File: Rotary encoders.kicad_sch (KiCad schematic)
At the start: 0 parts

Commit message: added encoder input connector
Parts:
- added C76, C77, C78: 100nF, 0_capacitors:C_0402_1005Metric, symbol 0_capacitors:CL05B104KO5NNNC
- added R69, R70, R71, R72: 10kΩ, 0_resistors:R_0402_1005Metric, symbol 0_resistors:0402WGF1002TCE
- added R73: 5.1kΩ, 0_resistors:R_0402_1005Metric, symbol 0_resistors:0402WGF5101TCE
- added R74: 47kΩ, 0_resistors:R_0402_1005Metric, symbol 0_resistors:0402WGF4702TCE
- added SW9: RotaryEncoder_Switch, Connector_JST:JST_PH_B5B-PH-K_1x05_P2.00mm_Vertical, symbol 0_modules:RotaryEncoder_Switch
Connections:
- new net: R70.2, R72.2, SW9.B
- new net: C78.1, R73.2, R74.2, SW9.S1
- new net: R69.2, R71.2, SW9.A
- new net +3.3V: R69.1, R70.1, R74.1
- new net BUTTON_ENCODER: R73.1
- new net GND: C76.2, C77.2, C78.2, SW9.C, SW9.S2
- new net TIM2_CH1: C76.1, R72.1
- new net TIM2_CH2: C77.1, R71.1
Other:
- title: (none) -> UI - Rotary encoders

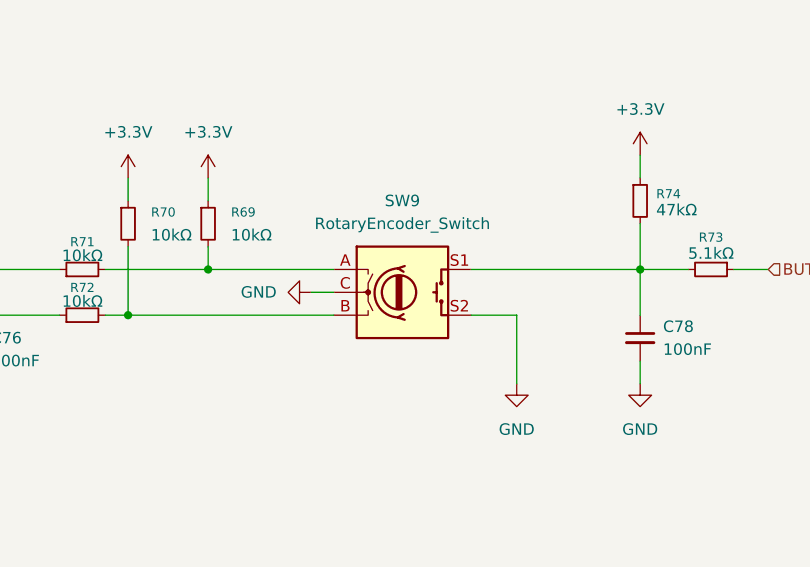
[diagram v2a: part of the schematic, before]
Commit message: duzo zmian, layout przetwornic i zasilania, wstepny routing sd card impedance control, usb differential impedance control
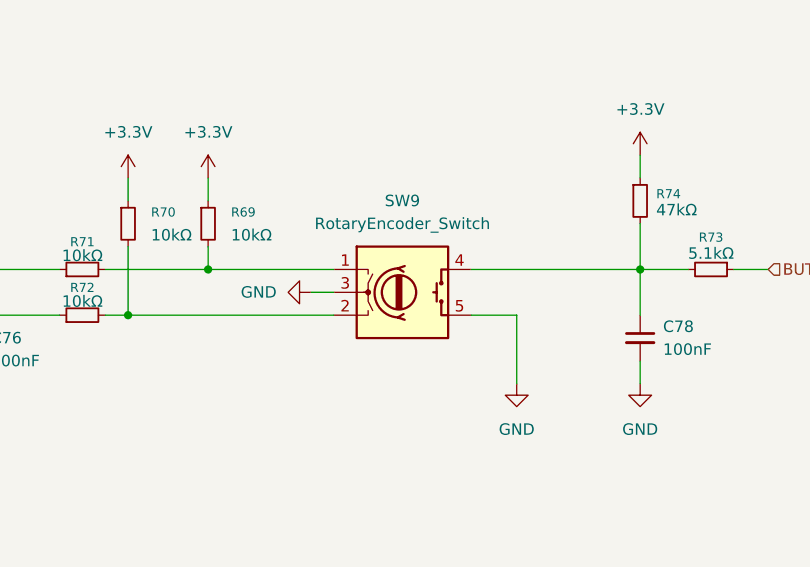
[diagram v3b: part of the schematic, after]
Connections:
- net GND: now also SW9.3, SW9.5; no longer SW9.C, SW9.S2
- net at R70.2, R72.2: now also SW9.2; no longer SW9.B
- net at C78.1, R73.2, R74.2: now also SW9.4; no longer SW9.S1
- net at R69.2, R71.2: now also SW9.1; no longer SW9.A
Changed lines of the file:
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@@
 			)
 		)
-		(pin "A"
+		(pin "3"
 		)
-		(pin "B"
+		(pin "2"
 		)
-		(pin "S2"
+		(pin "4"
 		)
-		(pin "C"
+		(pin "1"
 		)
-		(pin "S1"
+		(pin "5"
 		)
 		(instances

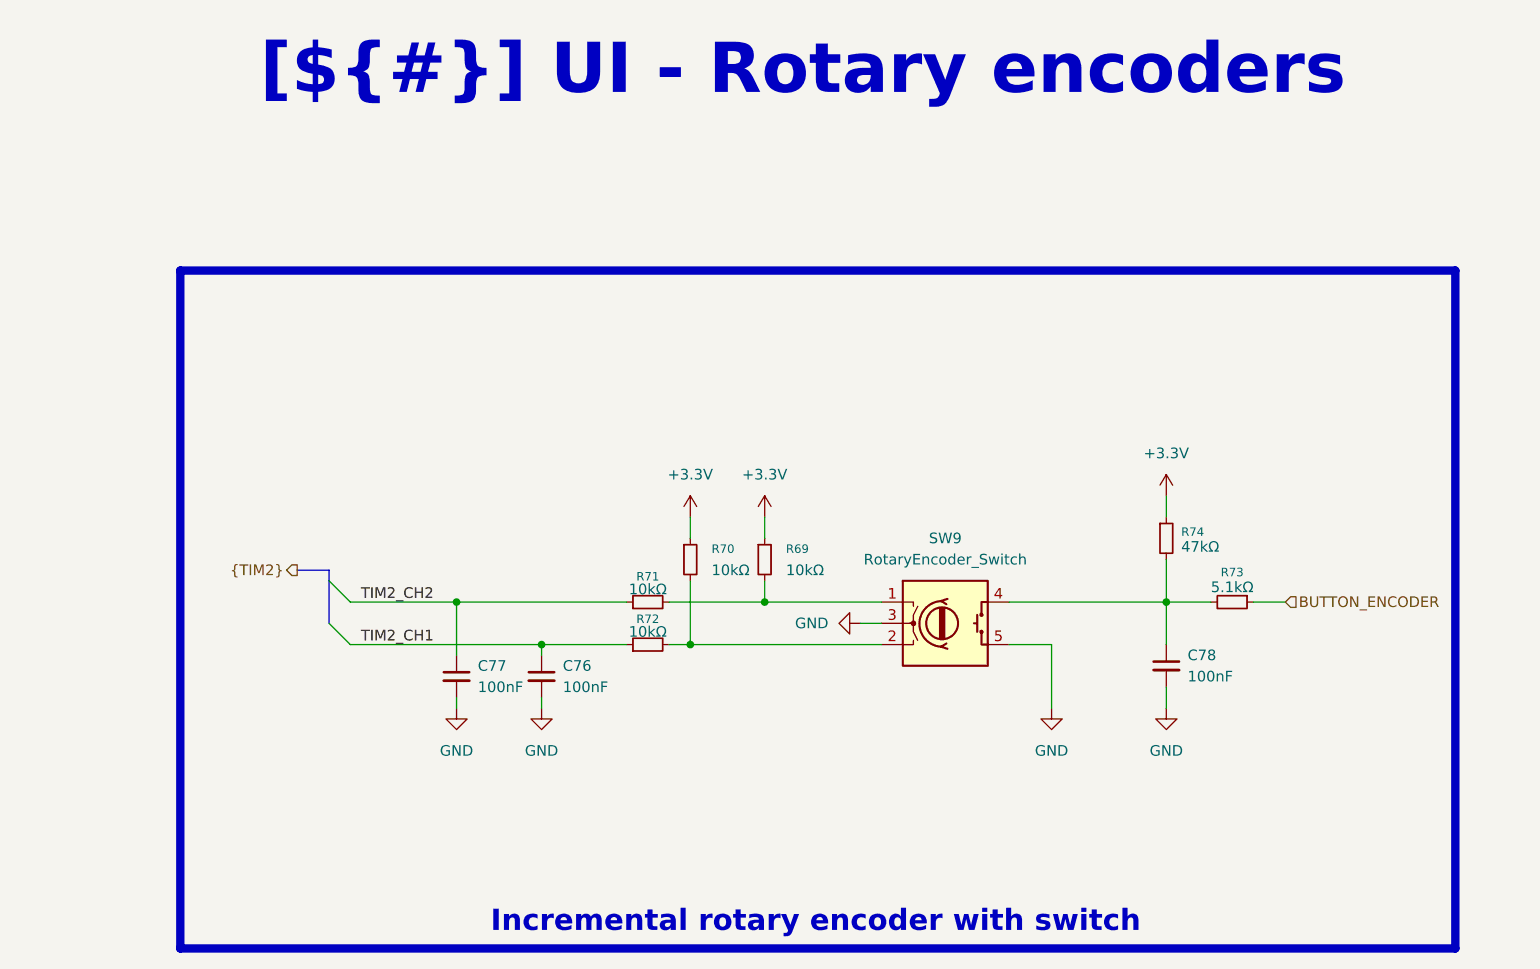
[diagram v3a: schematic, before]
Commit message: added tvs diodes to protect inputs + final component placement
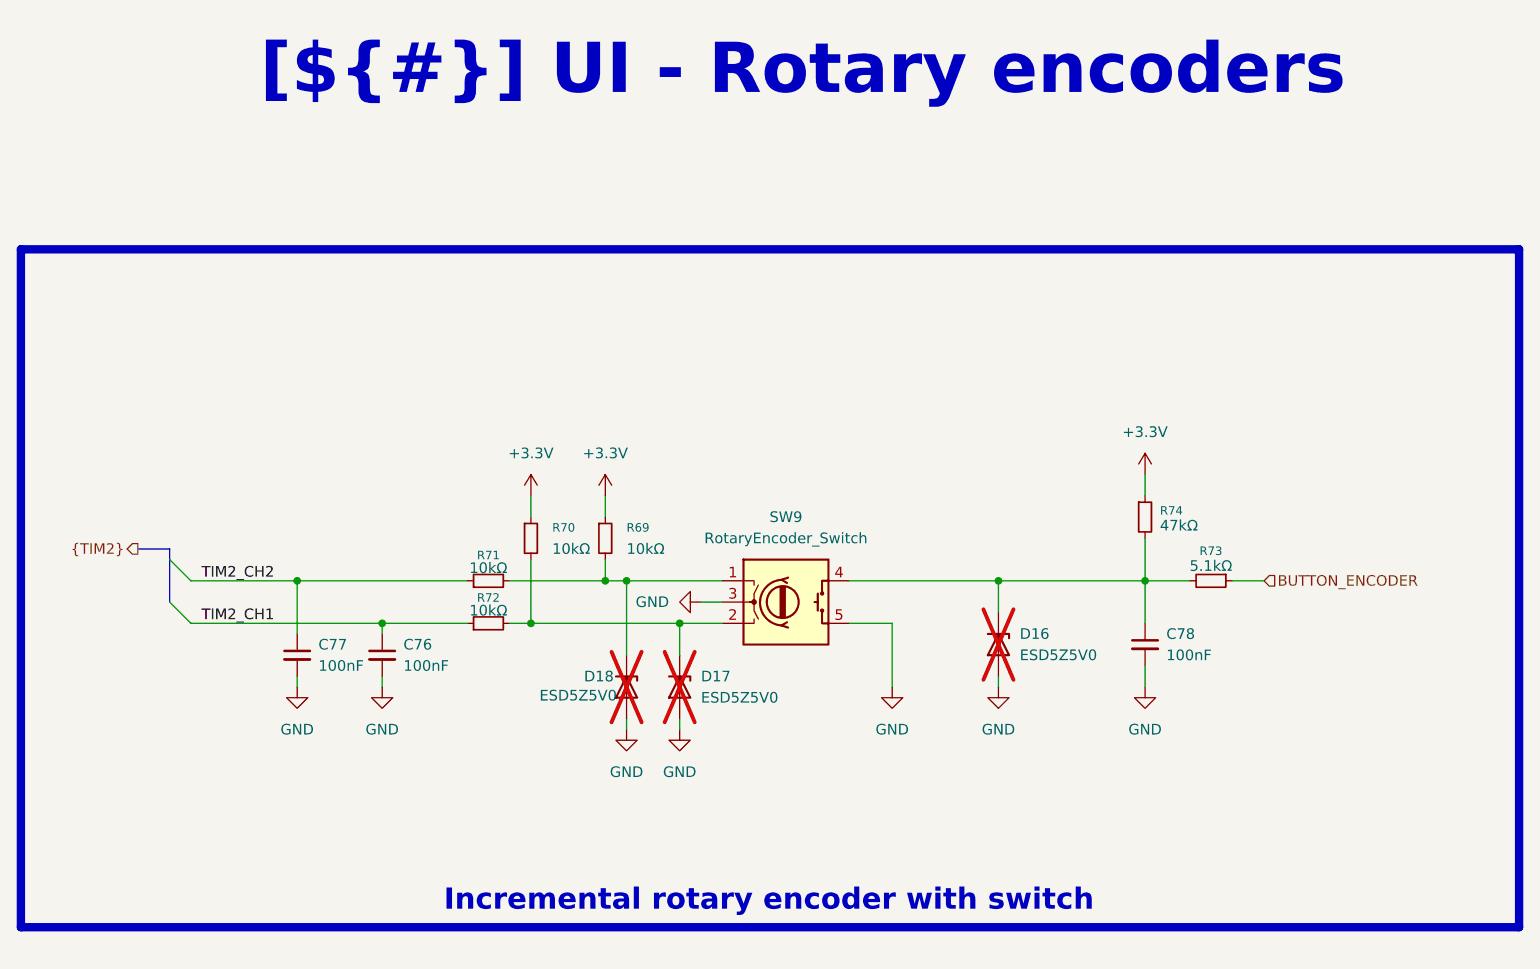
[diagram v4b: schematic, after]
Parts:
- added D16, D17, D18: ESD5Z5V0, 0_diodes:D_SOD-523, symbol 0_diodes:ESD5Z5V0
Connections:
- net GND: now also D16.2 (A), D17.2 (A), D18.2 (A)
- net at R70.2, R72.2, SW9.2: now also D17.1 (K)
- net at C78.1, R73.2, R74.2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: now also D16.1 (K)
- net at R69.2, R71.2, SW9.1: now also D18.1 (K)
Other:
- moved on the sheet: C76, C77, C78, R69, R70, R71, R72, R73, R74, SW9

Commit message: designator chagnes and cleanup silkscreen
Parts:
- C76, C77, C78: LCSC PN (none) -> C1525
- D16, D17, D18: LCSC PN (none) -> C191023
- R69, R70, R71, R72: LCSC PN (none) -> C25744
- R73: LCSC PN (none) -> C25905
- R74: LCSC PN (none) -> C25792
- SW9: LCSC PN (none) -> C157993
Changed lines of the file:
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@@
+			)
+		)
+		(property "LCSC PN" "C1525"
+			(at 97.79 88.9 0)
+			(effects
+				(font
+					(size 1.27 1.27)
+				)
+				(hide yes)
 			)
 		)
@@
 		)
 		(property "Supplier Part Number 1" "C25744"
+			(at 110.49 85.09 0)
+			(effects
+				(font
+					(size 1.27 1.27)
+				)
+				(hide yes)
+			)
+		)
+		(property "LCSC PN" "C25744"
 			(at 110.49 85.09 0)
 			(effects
@@
 			)
 		)
+		(property "LCSC PN" "C191023"
+			(at 171.45 87.63 0)
+			(effects
+				(font
+					(size 1.27 1.27)
+				)
+				(hide yes)
+			)
+		)
 		(pin "2"
 		)
@@
 			)
 		)
+		(property "LCSC PN" "C191023"
+			(at 127 92.71 0)
+			(effects
+				(font
+					(size 1.27 1.27)
+				)
+				(hide yes)
+			)
+		)
 		(pin "2"
 		)
@@
 		)
 		(property "Supplier Part Number 1" "C1525"
+			(at 87.63 88.9 0)
+			(effects
+				(font
+					(size 1.27 1.27)
+				)
+				(hide yes)
+			)
+		)
+		(property "LCSC PN" "C1525"
 			(at 87.63 88.9 0)
 			(effects
@@
 			)
 		)
+		(property "LCSC PN" "C191023"
+			(at 133.35 92.71 0)
+			(effects
+				(font
+					(size 1.27 1.27)
+				)
+				(hide yes)
+			)
+		)
 		(pin "2"
 		)
@@
 			)
 		)
+		(property "LCSC PN" "C25905"
+			(at 196.85 80.01 0)
+			(effects
+				(font
+					(size 1.27 1.27)
+				)
+				(hide yes)
+			)
+		)
 		(pin "2"
 		)
@@
 			)
 		)
+		(property "LCSC PN" "C157993"
+			(at 146.05 82.55 0)
+			(effects
+				(font
+					(size 1.27 1.27)
+				)
+				(hide yes)
+			)
+		)
 		(pin "3"
 		)
@@
 			)
 		)
+		(property "LCSC PN" "C25744"
+			(at 115.57 74.93 0)
+			(effects
+				(font
+					(size 1.27 1.27)
+				)
+				(hide yes)
+			)
+		)
 		(pin "1"
 		)
@@
 			)
 		)
+		(property "LCSC PN" "C25744"
+			(at 124.46 74.93 0)
+			(effects
+				(font
+					(size 1.27 1.27)
+				)
+				(hide yes)
+			)
+		)
 		(pin "1"
 		)
@@
 			)
 		)
+		(property "LCSC PN" "C25744"
+			(at 110.49 80.01 0)
+			(effects
+				(font
+					(size 1.27 1.27)
+				)
+				(hide yes)
+			)
+		)
 		(pin "1"
 		)
@@
 			)
 		)
+		(property "LCSC PN" "C25792"
+			(at 188.976 72.39 0)
+			(effects
+				(font
+					(size 1.27 1.27)
+				)
+				(hide yes)
+			)
+		)
 		(pin "1"
 		)
@@
 			(at 188.976 87.63 0)
 			(effects
+				(font
+					(size 1.27 1.27)
+				)
+				(hide yes)
+			)
+		)
+		(property "LCSC PN" "C1525"
+			(at 188.976 87.63 0)
+			(effects
